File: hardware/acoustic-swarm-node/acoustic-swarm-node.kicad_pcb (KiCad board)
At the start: 2 copper layers, 110 x 85 mm, 91 parts, among them J1 PIEZO/HV, J10 SWARM BFSK TX1, J11 ARM-SW (NC), J12 MODEM KONTAKTOR, J2 HIDROFON AFE, J3 AKUSTIK I2C, J4 SIZINTI PROBU, J5 AKUSTIK CH0 TX, J6 AKUSTIK CH1 TX, J7 AKUSTIK CH2 TX, J8 AKUSTIK CH3 TX, J9 SWARM BFSK TX0, Q1 AO3400A, Q2 BCP56-16, U1 LMR16006XDDCR, U2 AP2112K-3.3, U3 Teensy 4.1

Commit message: refactor: rename carrier project to acoustic-swarm-node and simplify docs
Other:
- board text added: "AKUSTIK SURU DUGUM KARTI REV A"
- board text removed: "PELAGOS AKUSTIK DUGUM KARTI REV A"

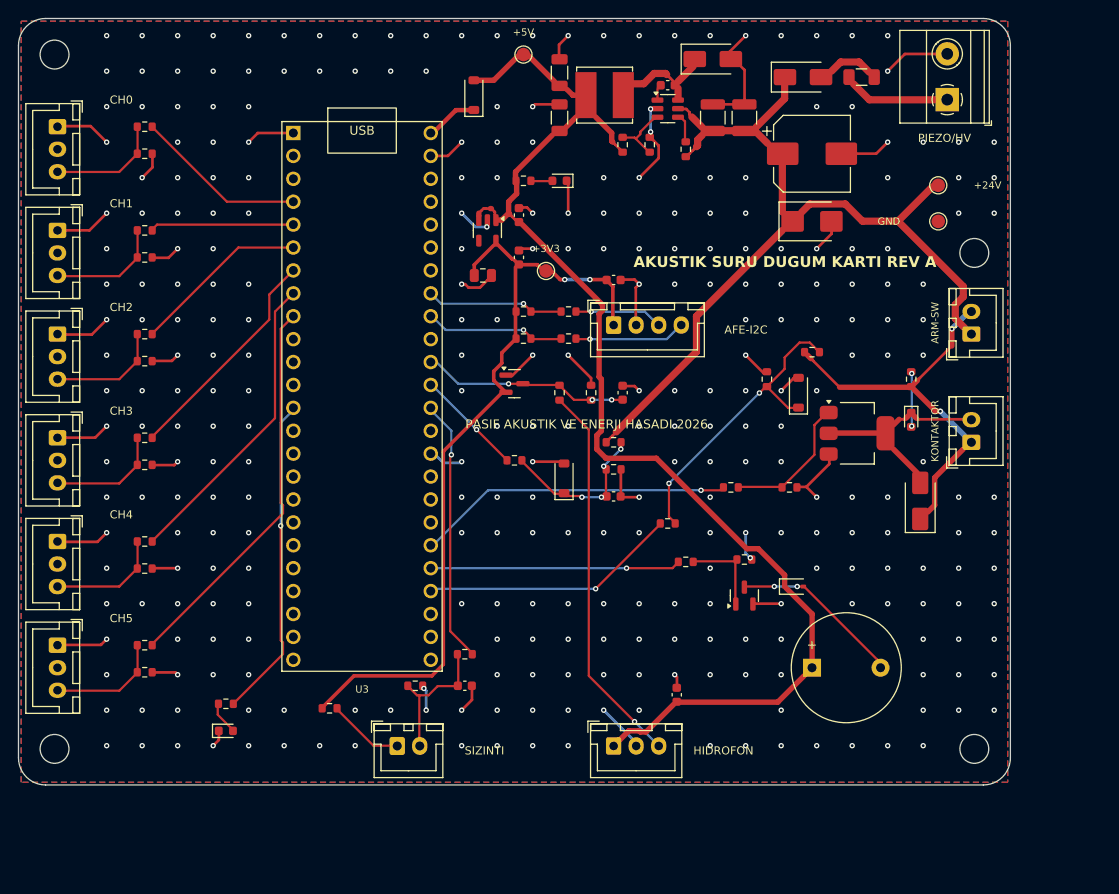
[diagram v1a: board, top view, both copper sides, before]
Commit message: Rev A acoustic node board, 192 kHz DSP chain and authenticated BFSK mesh
Hardware
- New netlist: always-on wake-up chain (MCP6042 60 dB + TLV7031 gating
  the LMR16006X enable), dual-gain hydrophone AFE (MCP6022, 40 kHz
  Sallen-Key), discrete piezo harvester, DRV8871 BFSK driver, switched
  battery divider and reed arming switch
- Board grows to 120x95 mm; Teensy pin map follows block placement
- Router: same-numbered pads are one target, reverse search and
  corridor waypoints for board-length nets, GND stitching routed last
- KiCad 9 support (kicad_env paths, multi-unit symbols, global labels);
  DRC 0 violations / 0 unconnected with schematic parity
- 3D renders and layout view under hardware/images

Firmware
- Streaming LOFAR (2 kHz) and DEMON (375 Hz) processors on 192 kHz
  dual-ADC DMA input, dual-gain channel selection
- Goertzel BFSK receiver with 4 timing lanes and out-of-band energy gate
- SipHash-2-4 tagged 20-byte mesh frame (replaces 16-bit FNV tag)
- PowerManager state machine around PWR_HOLD / wake latch
- Host tests: dsp, bfsk_modem, swarm_mesh, power_manager (ASan/UBSan)

Model
- dsp/node_model.py derives AFE response, sleep current and link budget
  from design.py values and checks them against firmware constants
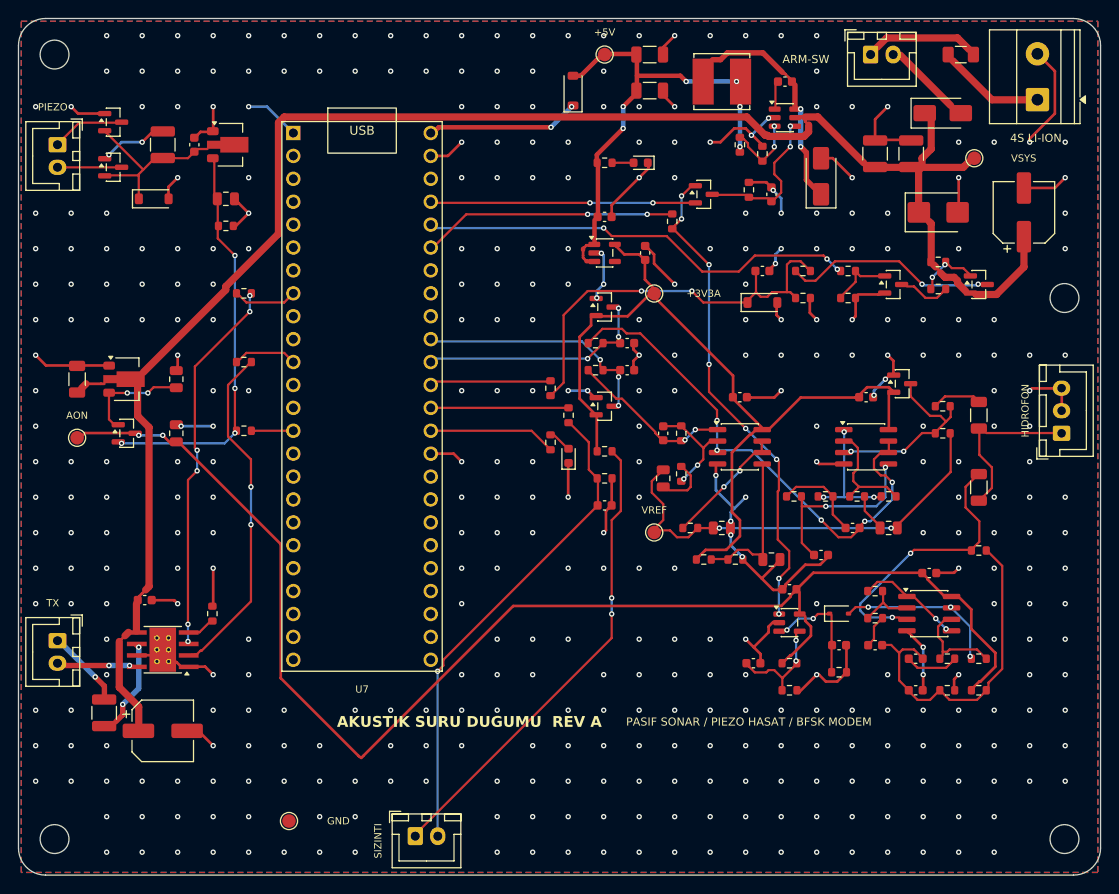
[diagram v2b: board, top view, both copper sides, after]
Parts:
- removed BZ1: 5V aktif, Buzzer_Beeper:Buzzer_12x9.5RM7.6
- removed C10: 100nF, Capacitor_SMD:C_0603_1608Metric
- removed J10: SWARM BFSK TX1, Connector_JST:JST_XH_B3B-XH-A_1x03_P2.50mm_Vertical
- removed J11: ARM-SW (NC), Connector_JST:JST_XH_B2B-XH-A_1x02_P2.50mm_Vertical
- removed J12: MODEM KONTAKTOR, Connector_JST:JST_XH_B2B-XH-A_1x02_P2.50mm_Vertical
- removed J7: AKUSTIK CH2 TX, Connector_JST:JST_XH_B3B-XH-A_1x03_P2.50mm_Vertical
- removed J8: AKUSTIK CH3 TX, Connector_JST:JST_XH_B3B-XH-A_1x03_P2.50mm_Vertical
- removed J9: SWARM BFSK TX0, Connector_JST:JST_XH_B3B-XH-A_1x03_P2.50mm_Vertical
- added C15: 1uF, Capacitor_SMD:C_0603_1608Metric, F.Cu at (149.5, 121.0)
- added C16: 100nF, Capacitor_SMD:C_0603_1608Metric, F.Cu at (151.0, 111.5)
- added C17: 470nF, Capacitor_SMD:C_0603_1608Metric, F.Cu at (141.0, 119.5)
- added C18: 100nF, Capacitor_SMD:C_0603_1608Metric, F.Cu at (131.5, 121.5)
- added C19: 100nF, Capacitor_SMD:C_0603_1608Metric, F.Cu at (135.5, 113.3)
- added C20: 1uF, Capacitor_SMD:C_0603_1608Metric, F.Cu at (133.5, 69.5)
- added C21: 100nF 25V, Capacitor_SMD:C_0603_1608Metric, F.Cu at (135.0, 57.0)
- added C22: 22uF 10V, Capacitor_SMD:C_1206_3216Metric, F.Cu at (120.0, 54.0)
- added C23: 22uF 10V, Capacitor_SMD:C_1206_3216Metric, F.Cu at (120.0, 58.0)
- added C24: 1uF, Capacitor_SMD:C_0603_1608Metric, F.Cu at (115.0, 72.0)
- added C25: 1uF, Capacitor_SMD:C_0603_1608Metric, F.Cu at (119.5, 76.0)
- added C26: 10uF, Capacitor_SMD:C_0805_2012Metric, F.Cu at (133.5, 110.0)
- added C27: 10uF, Capacitor_SMD:C_0805_2012Metric, F.Cu at (128.0, 106.5)
- added C28: 100nF, Capacitor_SMD:C_1206_3216Metric, F.Cu at (156.5, 94.0)
- added C29: 10uF, Capacitor_SMD:C_0805_2012Metric, F.Cu at (146.5, 106.5)
- added C30: 2.2nF, Capacitor_SMD:C_0603_1608Metric, F.Cu at (142.5, 106.5)
- added C31: 1nF, Capacitor_SMD:C_0603_1608Metric, F.Cu at (139.0, 109.5)
- added C32: 100nF, Capacitor_SMD:C_0603_1608Metric, F.Cu at (144.0, 92.0)
- added C33: 270pF, Capacitor_SMD:C_0603_1608Metric, F.Cu at (121.5, 96.0)
- added C34: 10uF, Capacitor_SMD:C_0805_2012Metric, F.Cu at (121.5, 101.0)
- added C35: 100nF, Capacitor_SMD:C_0603_1608Metric, F.Cu at (130.0, 92.0)
- added C36: 2.2nF, Capacitor_SMD:C_0603_1608Metric, F.Cu at (117.5, 86.0)
- added C37: 2.2nF, Capacitor_SMD:C_0603_1608Metric, F.Cu at (117.5, 89.0)
- added C38: 47uF 35V, Capacitor_SMD:CP_Elec_6.3x7.7, F.Cu at (66.0, 129.0)
- added C39: 100nF 50V, Capacitor_SMD:C_0603_1608Metric, F.Cu at (64.0, 114.5)
- added C40: 2.2uF 50V, Capacitor_SMD:C_1210_3225Metric, F.Cu at (59.5, 127.0)
- added C41: 100nF, Capacitor_SMD:C_0603_1608Metric, F.Cu at (115.0, 104.0)
- added D13: MAVI, LED_SMD:LED_0603_1608Metric, F.Cu at (111.0, 98.5)
- added D14: BAT54S, Package_TO_SOT_SMD:SOT-23, F.Cu at (60.5, 61.5)
- added D15: BAT54S, Package_TO_SOT_SMD:SOT-23, F.Cu at (60.5, 66.5)
- added D16: BZT52C18, Diode_SMD:D_SOD-123, F.Cu at (65.0, 70.0)
- added R38: 100, Resistor_SMD:R_0603_1608Metric, F.Cu at (75.0, 88.1)
- added R39: 62k, Resistor_SMD:R_0603_1608Metric, F.Cu at (71.5, 116.0)
- added R40: 10k, Resistor_SMD:R_0603_1608Metric, F.Cu at (115.0, 98.0)
- added R41: 47k, Resistor_SMD:R_0603_1608Metric, F.Cu at (115.0, 101.0)
- added R42: 1k, Resistor_SMD:R_0603_1608Metric, F.Cu at (111.0, 94.0)
- added R43: 330, Resistor_SMD:R_0603_1608Metric, F.Cu at (109.0, 97.0)
- added R44: 1M, Resistor_SMD:R_0603_1608Metric, F.Cu at (73.0, 73.0)
- added TP5: +3V3_AON, TestPoint:TestPoint_Pad_D1.5mm, F.Cu at (56.5, 96.5)
- added TP6: VREF_A, TestPoint:TestPoint_Pad_D1.5mm, F.Cu at (120.5, 107.0)
- added U10: DRV8871, Package_SO:Texas_HTSOP-8-1EP_3.9x4.9mm_P1.27mm_EP2.95x4.9mm_Mask2.4x3.1mm_ThermalVias, F.Cu at (66.0, 120.0)
- added U4: TLV7031, Package_TO_SOT_SMD:SOT-23-5, F.Cu at (135.5, 117.0)
- added U5: LMR16006XDDCR, Package_TO_SOT_SMD:SOT-23-6, F.Cu at (135.0, 61.0)
- added U6: LP5907MFX-3.3, Package_TO_SOT_SMD:SOT-23-5, F.Cu at (115.0, 76.0)
- added U7: Teensy 4.1, acoustic:Teensy4.1_Socket, F.Cu at (80.5, 62.7)
- added U8: MCP6022, Package_SO:SOIC-8_3.9x4.9mm_P1.27mm, F.Cu at (144.0, 97.5)
- added U9: MCP6022, Package_SO:SOIC-8_3.9x4.9mm_P1.27mm, F.Cu at (130.0, 97.5)
- C1: value 47uF 63V -> 47uF 35V; footprint Capacitor_SMD:CP_Elec_8x10 -> Capacitor_SMD:CP_Elec_6.3x7.7
- C11: value 100nF -> 10uF; footprint Capacitor_SMD:C_0603_1608Metric -> Capacitor_SMD:C_0805_2012Metric
- C13: footprint Capacitor_SMD:C_0603_1608Metric -> Capacitor_SMD:C_1206_3216Metric
- C14: value 100nF -> 1uF
- C2, C3: value 2.2uF 100V -> 2.2uF 50V
- C4: value 100nF 25V -> 100nF
- C5: value 22uF 10V -> 1uF 50V
- C6: value 22uF 10V -> 4.7uF; footprint Capacitor_SMD:C_1206_3216Metric -> Capacitor_SMD:C_0805_2012Metric
- C7: value 1uF -> 22uF 25V; footprint Capacitor_SMD:C_0603_1608Metric -> Capacitor_SMD:C_1210_3225Metric
- C8: value 1uF -> 100nF 50V
- C9: value 10uF -> 4.7uF
- D1: value SS16 -> SS26
- D10: value SS16 -> BAT54S; footprint Diode_SMD:D_SMA -> Package_TO_SOT_SMD:SOT-23
- D11: value KIRMIZI -> BAT54S; footprint LED_SMD:LED_0603_1608Metric -> Package_TO_SOT_SMD:SOT-23
- D12: value BZT52C3V3 -> BAT54S; footprint Diode_SMD:D_SOD-123 -> Package_TO_SOT_SMD:SOT-23
- D2: value SMBJ30CA -> SMBJ20CA
- D3: value SS16 -> BZT52C3V3; footprint Diode_SMD:D_SMA -> Diode_SMD:D_SOD-123
- D4: value B5819W -> BAT54C; footprint Diode_SMD:D_SOD-123 -> Package_TO_SOT_SMD:SOT-23
- D5: value YESIL -> BAT54WS; footprint LED_SMD:LED_0603_1608Metric -> Diode_SMD:D_SOD-323
- D6: value BAT54S -> BAT54C
- D7: value BZT52C3V3 -> SS16; footprint Diode_SMD:D_SOD-123 -> Diode_SMD:D_SMA
- D8: value 1N4148W -> YESIL; footprint Diode_SMD:D_SOD-323 -> LED_SMD:LED_0603_1608Metric
- D9: value MAVI -> B5819W; footprint LED_SMD:LED_0603_1608Metric -> Diode_SMD:D_SOD-123
- F1: value 1A 63V -> 2A 63V
- H1, H2, H3, H4: value CH3 -> M3
- J1: value PIEZO/HV -> 4S LI-ION
- J2: value HIDROFON AFE -> ARM-SW (NC); footprint Connector_JST:JST_XH_B3B-XH-A_1x03_P2.50mm_Vertical -> Connector_JST:JST_XH_B2B-XH-A_1x02_P2.50mm_Vertical
- J3: value AKUSTIK I2C -> PIEZO; footprint Connector_JST:JST_XH_B4B-XH-A_1x04_P2.50mm_Vertical -> Connector_JST:JST_XH_B2B-XH-A_1x02_P2.50mm_Vertical
- J4: value SIZINTI PROBU -> HIDROFON; footprint Connector_JST:JST_XH_B2B-XH-A_1x02_P2.50mm_Vertical -> Connector_JST:JST_XH_B3B-XH-A_1x03_P2.50mm_Vertical
- J5: value AKUSTIK CH0 TX -> TRANSDUSOR; footprint Connector_JST:JST_XH_B3B-XH-A_1x03_P2.50mm_Vertical -> Connector_JST:JST_XH_B2B-XH-A_1x02_P2.50mm_Vertical
- J6: value AKUSTIK CH1 TX -> SIZINTI PROBU; footprint Connector_JST:JST_XH_B3B-XH-A_1x03_P2.50mm_Vertical -> Connector_JST:JST_XH_B2B-XH-A_1x02_P2.50mm_Vertical
- Q1: value AO3400A -> AO3401A
- Q2: value BCP56-16 -> 2N7002; footprint Package_TO_SOT_SMD:SOT-223-3_TabPin2 -> Package_TO_SOT_SMD:SOT-23
- R10, R9: value 220 -> 10M
- R11: value 100k -> 10M
- R12, R14: value 100k -> 1M
- R13, R15: value 100k -> 33k
- R16: value 100k -> 4.7M
- R17: value 4.7k -> 4.7M
- R18: value 4.7k -> 5.1M
- R19: value 33 -> 10k
- R2: value 54.9k -> 100k
- R20: value 33 -> 1M
- R21: value 10k -> 54.9k
- R23: value 10k -> 2.2k
- R24: value 47k -> 10k
- R25: value 1k -> 10k
- R26: value 68k -> 49.9
- R27, R30: value 10k -> 1k
- R28: value 1k -> 10M
- R29: value 470 -> 9.1k
- R3: value 10k -> 100
- R31: value 10k -> 2.7k
- R32: value 47k -> 2.7k
- R33: value 10k -> 9.1k
- R36: value 100k -> 100
- R37: value 330 -> 100
- R4: value 2.2k -> 100k
- R5: value 220 -> 100k
- R6: value 220 -> 15k
- R7: value 220 -> 1k
- R8: value 220 -> 10k
- TP1: value +24V -> VSYS
- TP3: value +3V3 -> +3V3A
- U1: value LMR16006XDDCR -> HT7533-1; footprint Package_TO_SOT_SMD:SOT-23-6 -> Package_TO_SOT_SMD:SOT-89-3
- U2: value AP2112K-3.3 -> HT7533-1; footprint Package_TO_SOT_SMD:SOT-23-5 -> Package_TO_SOT_SMD:SOT-89-3
- U3: value Teensy 4.1 -> MCP6042; footprint stingray:Teensy4.1_Socket -> Package_SO:SOIC-8_3.9x4.9mm_P1.27mm
- moved R11 102.4 mm to (156.5, 109.0)
- moved TP4 98.0 mm to (80.0, 139.0)
- moved R14 95.0 mm to (156.5, 121.0)
- moved R9 94.0 mm to (156.5, 124.5), turned to 0 degrees
- moved R15 89.6 mm to (153.0, 121.0)
- moved R10 89.1 mm to (153.0, 124.5), turned to 0 degrees
- moved R12 89.1 mm to (145.0, 113.5)
- moved U3 88.4 mm to (151.0, 116.0)
- moved R13 85.9 mm to (145.0, 116.5)
- moved J2 81.8 mm to (144.5, 54.0)
- moved J4 81.4 mm to (165.7, 96.0), turned to 90 degrees
- moved D9 80.8 mm to (111.5, 58.0), turned to 90 degrees
- moved J6 78.0 mm to (94.0, 140.7), turned to 0 degrees
- moved R16 77.0 mm to (141.0, 122.5)
- moved R5 74.7 mm to (137.0, 78.0), turned to 0 degrees
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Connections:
- C1 pad 1: +24V -> VSYS
- C11 pad 1: T_DEPTH_ADC -> +3V3_AON
- C12 pad 1: +5V -> VREF_W
- C13 pad 1: LEAK_NODE -> HYD_SIG
- C13 pad 2: GND -> W_IN
- C14 pad 1: BATT_DIV -> W_G1
- C14 pad 2: GND -> VREF_W
- C2 pad 1: +24V -> VSYS
- C3 pad 1: +24V -> VSYS
- C4 pad 1: BUCK_CB -> BATT_DIV
- C4 pad 2: BUCK_SW -> GND
- C5 pad 1: +5V -> VSYS
- C6 pad 1: +5V -> +3V3_LDO
- C7 pad 1: +5V -> HV_STORE
- C8 pad 1: +3V3 -> HV_STORE
- C9 pad 1: +3V3 -> V_HARV
- D1 pad 1: +24V -> VSYS
- D1 pad 2: VBAT_F -> ARM_RET
- D10 pad 1: KILL_RET -> GND
- D10 pad 2: COIL_N -> +3V3A
- D11 pad 1: COIL_N -> GND
- D11 pad 2: LED_ESC_A -> +3V3A
- D12 pad 1: KILL_DIV -> GND
- D12 pad 2: GND -> +3V3A
- D2 pad 1: +24V -> VSYS
- D3 pad 1: BUCK_SW -> BATT_DIV
- D4 pad 1: TEENSY_VIN -> +3V3_LDO
- D4 pad 2: +5V -> V_HARV
- D5 pad 1: GND -> W_ENV
- D5 pad 2: LED_PWR_A -> W_B
- D6 pad 1: GND -> WAKE_CMP
- D6 pad 2: +3V3 -> T_PWR_HOLD
- D6 pad 3: T_DEPTH_ADC -> BUCK_EN
- D7 pad 1: BATT_DIV -> BUCK_SW
- D8 pad 1: +5V -> GND
- D8 pad 2: BUZ_N -> LED_PWR_A
- D9 pad 1: GND -> TEENSY_VIN
- D9 pad 2: LED_STAT_A -> +5V
- J2 pad 1: +5V -> VBAT_F
- J2 pad 2: GND -> ARM_RET
- J3 pad 1: +3V3 -> PZ1
- J3 pad 2: GND -> PZ2
- J4 pad 1: LEAK_P -> HYD_SIG
- J4 pad 2: LEAK_NODE -> GND
- J5 pad 1: GND -> TX_P
- J5 pad 2: (no net) -> TX_OUT2
- J6 pad 1: GND -> LEAK_P
- J6 pad 2: (no net) -> LEAK_NODE
- Q1 pad 1: Q1_G -> BS_G
- Q1 pad 2: GND -> VSYS
- Q1 pad 3: BUZ_N -> BATT_SW
- Q2 pad 1: Q2_B -> BS_EN_G
- Q2 pad 2: COIL_N -> GND
- Q2 pad 3: GND -> BS_D
- R1 pad 1: +24V -> VSYS
- R1 pad 2: BUCK_SHDN -> BS_G
- R10 pad 1: T_PWM5 -> VREF_W
- R10 pad 2: ESC_PWM5 -> GND
- R11 pad 1: ESC_PWM0 -> W_IN
- R11 pad 2: GND -> VREF_W
- R12 pad 1: ESC_PWM1 -> W_A
- R12 pad 2: GND -> W_FB1
- R13 pad 1: ESC_PWM2 -> W_FB1
- R13 pad 2: GND -> W_G1
- R14 pad 1: ESC_PWM3 -> W_B
- R14 pad 2: GND -> W_FB2
- R15 pad 1: ESC_PWM4 -> W_FB2
- R15 pad 2: GND -> W_G2
- R16 pad 1: ESC_PWM5 -> W_ENV
- R17 pad 1: +3V3 -> +3V3_AON
- R17 pad 2: T_SCL0 -> W_TH
- R18 pad 1: +3V3 -> W_TH
- R18 pad 2: T_SDA0 -> GND
- R19 pad 1: T_SCL0 -> WAKE_CMP
- R19 pad 2: IMU_SCL -> T_WAKE
- R2 pad 1: +5V -> BS_G
- R2 pad 2: BUCK_FB -> BS_D
- R20 pad 1: T_SDA0 -> BUCK_EN
- R20 pad 2: IMU_SDA -> GND
- R21 pad 1: DEPTH_RAW -> +5V
- R21 pad 2: T_DEPTH_ADC -> BUCK_FB
- R22 pad 1: T_DEPTH_ADC -> BUCK_FB
- R23 pad 1: +3V3 -> +5V
- R23 pad 2: LEAK_P -> LED_PWR_A
- R24 pad 1: LEAK_NODE -> +3V3A
- R24 pad 2: GND -> VREF_DIV
- R25 pad 1: LEAK_NODE -> VREF_DIV
- R25 pad 2: T_LEAK_ADC -> GND
- R26 pad 1: +24V -> VREF_BUF
- R26 pad 2: BATT_DIV -> VREF_A
- R27 pad 1: BATT_DIV -> A_IN
- R27 pad 2: GND -> A_INP
- R28 pad 1: BATT_DIV -> A_INP
- R28 pad 2: T_BATT_ADC -> VREF_A
- R29 pad 1: T_ESC_EN -> A_S1
- R29 pad 2: Q2_B -> A_FB1
- R3 pad 1: BUCK_FB -> T_BATT_EN
- R3 pad 2: GND -> BS_EN_G
- R30 pad 1: Q2_B -> A_FB1
- R30 pad 2: GND -> A_G1
- R31 pad 1: KILL_RET -> A_S1
- R31 pad 2: LED_ESC_A -> A_SK1
- R32 pad 1: KILL_RET -> A_SK1
- R32 pad 2: KILL_DIV -> A_SK2
- R33 pad 1: KILL_DIV -> AFE_HI
- R33 pad 2: GND -> A_FB2
- R34 pad 1: KILL_DIV -> A_FB2
- R34 pad 2: T_KILL_SENSE -> A_G2
- R35 pad 1: T_BUZZER -> AFE_LO
- R35 pad 2: Q1_G -> T_ADC_LO
- R36 pad 1: Q1_G -> AFE_HI
- R36 pad 2: GND -> T_ADC_HI
- R37 pad 1: T_LED -> T_TX_IN1
- R37 pad 2: LED_STAT_A -> TX_IN1
- R4 pad 1: +5V -> BS_EN_G
- R4 pad 2: LED_PWR_A -> GND
- R5 pad 1: T_PWM0 -> BATT_SW
- R5 pad 2: ESC_PWM0 -> BATT_DIV
- R6 pad 1: T_PWM1 -> BATT_DIV
- R6 pad 2: ESC_PWM1 -> GND
- R7 pad 1: T_PWM2 -> BATT_DIV
- R7 pad 2: ESC_PWM2 -> T_BATT_ADC
- R8 pad 1: T_PWM3 -> V_HARV
- R8 pad 2: ESC_PWM3 -> T_HARV_PG
- R9 pad 1: T_PWM4 -> +3V3_AON
- R9 pad 2: ESC_PWM4 -> VREF_W
- TP1 pad 1: +24V -> VSYS
- TP3 pad 1: +3V3 -> +3V3A
- U1 pad 1: BUCK_CB -> GND
- U1 pad 2: GND -> VSYS
- U1 pad 3: BUCK_FB -> +3V3_LDO
- U2 pad 1: +5V -> GND
- U2 pad 2: GND -> HV_STORE
- U2 pad 3: +5V -> V_HARV
- U3 pad 1: GND -> W_A
- U3 pad 2: (no net) -> W_FB1
- U3 pad 3: (no net) -> W_IN
- U3 pad 4: T_PWM0 -> GND
- U3 pad 5: T_PWM1 -> W_A
- U3 pad 6: T_PWM2 -> W_FB2
- U3 pad 7: T_PWM3 -> W_B
- U3 pad 8: T_PWM4 -> +3V3_AON
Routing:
- net VSYS: track 0.00 -> 193.7 mm
- net +3V3_AON: track 0.00 -> 149.9 mm, vias 0 -> 2
- net +24V: track 92.4 -> 0.00 mm
- net +3V3A: track 0.00 -> 87.2 mm
- net +3V3: track 84.0 -> 0.00 mm, vias 2 -> 0
- net +5V: track 128.4 -> 47.5 mm, vias 0 -> 6
- net GND: track 184.9 -> 247.4 mm, vias 310 -> 403
- net AFE_LO: track 0.00 -> 56.4 mm, vias 0 -> 5
- net WAKE_CMP: track 0.00 -> 53.5 mm, vias 0 -> 8
- net T_BATT_EN: track 0.00 -> 48.2 mm, vias 0 -> 3
- net VREF_A: track 0.00 -> 46.3 mm, vias 0 -> 2
- net LEAK_P: track 8.02 -> 51.9 mm, vias 0 -> 2
- net V_HARV: track 0.00 -> 43.2 mm, vias 0 -> 4
- net T_PWM5: track 42.6 -> 0.00 mm
- net DEPTH_RAW: track 42.4 -> 0.00 mm, vias 1 -> 0
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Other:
- board size 110 x 85 mm -> 120 x 95 mm
- board text added: "+3V3A"
- board text added: "4S LI-ION"
- board text added: "AKUSTIK SURU DUGUMU REV A"
- board text added: "AON"
- board text added: "PASIF SONAR / PIEZO HASAT / BFSK MODEM"
- board text added: "PIEZO"
- board text added: "TX"
- board text added: "VREF"
- board text added: "VSYS"
- board text removed: "+24V"
- board text removed: "+3V3"
- board text removed: "AFE-I2C"
- board text removed: "AKUSTIK SURU DUGUM KARTI REV A"
- board text removed: "CH0"
- board text removed: "CH1"
- board text removed: "CH2"
- board text removed: "CH3"
- board text removed: "CH4"
- board text removed: "CH5"
- board text removed: "KONTAKTOR"
- board text removed: "PASIF AKUSTIK VE ENERJI HASADI 2026"
- board text removed: "PIEZO/HV"
